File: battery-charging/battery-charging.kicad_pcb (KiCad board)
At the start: 2 copper layers, 38 x 16.8 mm, 20 parts, among them J101 USB_B_Micro, J102 BAT-, J103 BAT+, U101 TC4056A, U102 MT3608

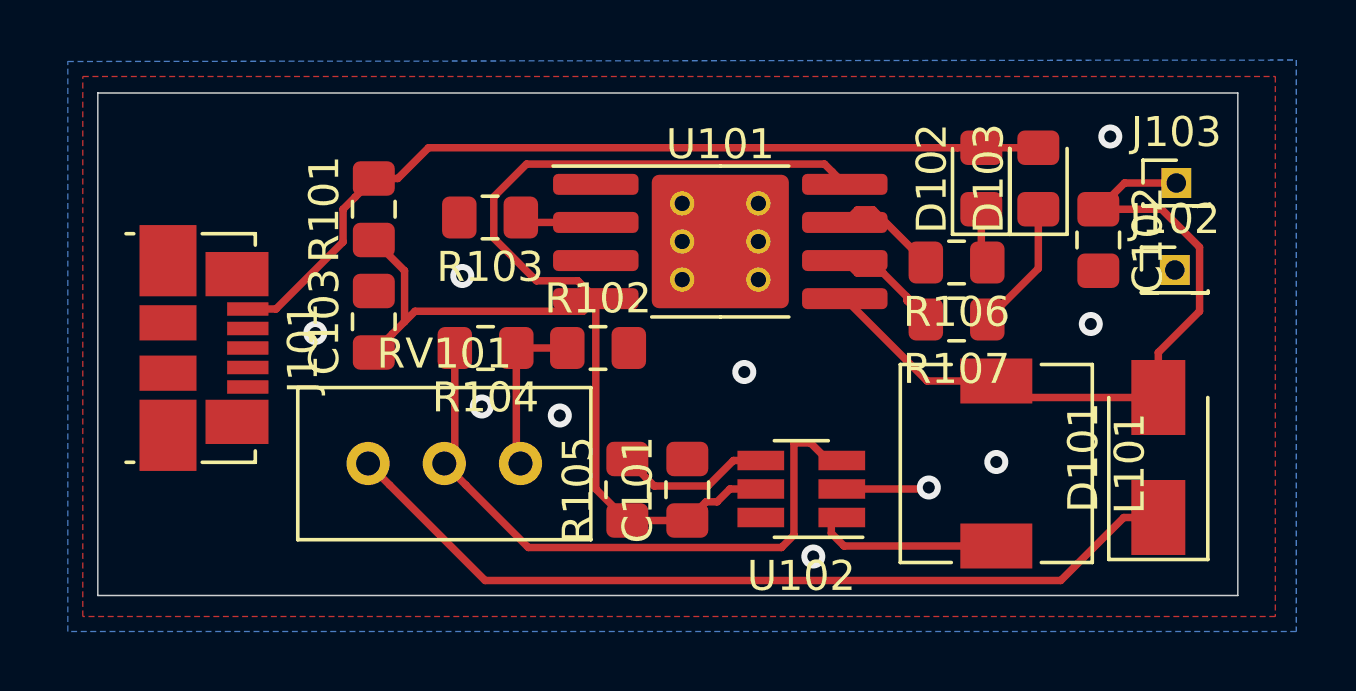
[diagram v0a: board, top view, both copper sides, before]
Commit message: added C167321 usb c
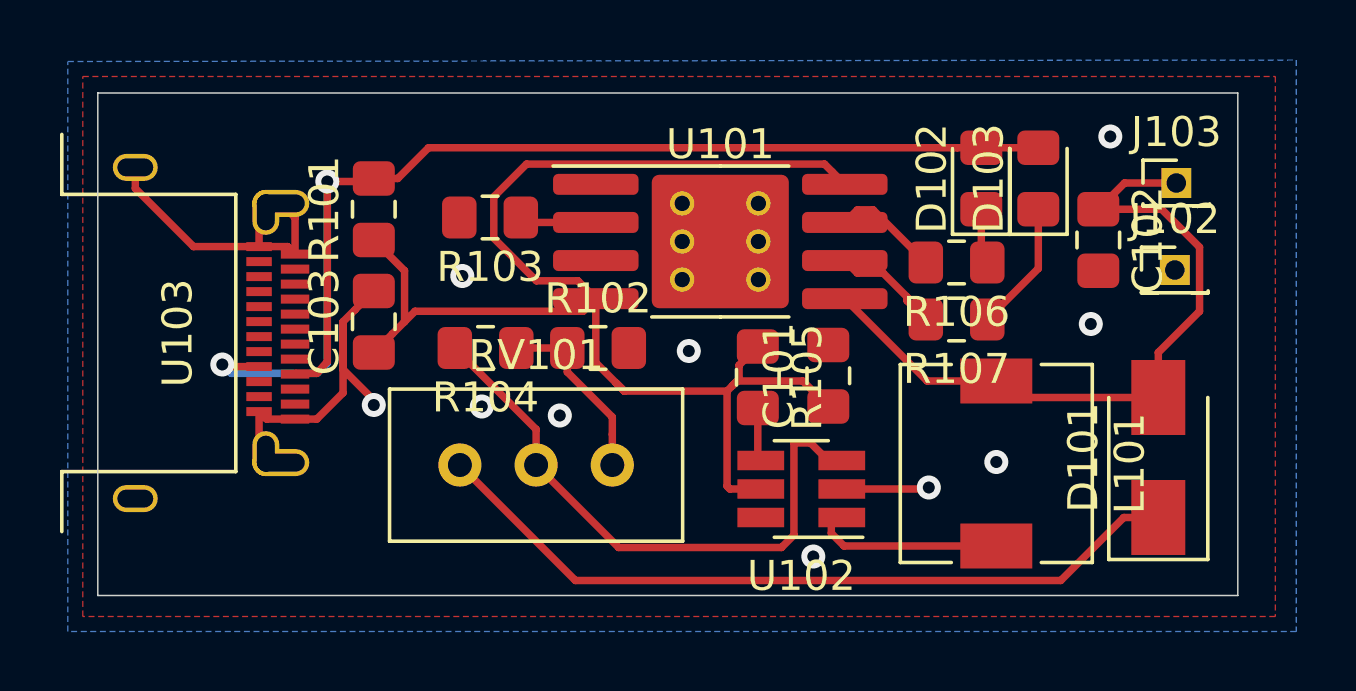
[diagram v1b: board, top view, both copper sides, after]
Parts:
- removed J101: USB_B_Micro, Connector_USB:USB_Micro-B_Molex_47346-0001
- added U103: C168692, water-lib:C168692, F.Cu at (45.3, 118.0)
- moved C101 6.04 mm to (68.4, 119.5)
- moved R105 5.74 mm to (66.0, 119.5), turned to 270 degrees
- moved RV101 3.06 mm to (61.2, 122.5)
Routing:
- net GND: track 2.92 -> 25.3 mm
- net VCC: track 29.2 -> 42.5 mm, vias 0 -> 2
- net +5V: track 42.1 -> 46.5 mm
- net Net-(R105-Pad2): track 5.17 -> 1.79 mm
- net +3V3: track 28.8 -> 25.7 mm
- net Net-(R104-Pad2): track 21.9 -> 19.8 mm
- net Net-(R102-Pad1): track 5.61 -> 6.22 mm

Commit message: battery changing urb c
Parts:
- U103: value C168692 -> C167321; footprint water-lib:C168692 -> water-lib:C167321
- moved U103 4.45 mm to (49.8, 118.2)
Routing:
- net VCC: track 42.5 -> 32.3 mm, vias 2 -> 0
- net GND: track 25.3 -> 15.6 mm, vias 10 -> 12
- net +5V: track 46.5 -> 47.7 mm
